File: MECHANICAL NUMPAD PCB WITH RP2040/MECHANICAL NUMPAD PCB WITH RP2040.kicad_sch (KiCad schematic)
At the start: 77 parts, among them IC2 RP2040_QFN56, SW1 SW_Push, SW10 SW_Push, SW11 SW_Push, SW12 SW_Push, SW13 SW_Push, SW14 SW_Push, SW15 SW_Push, SW16 SW_Push, SW17 SW_Push, SW18 SW_Push, SW19 SW_Push, SW2 SW_Push, SW20 SW_Push, SW21 KMR2, SW22 KMR2, SW3 SW_Push, SW4 SW_Push, SW5 SW_Push, SW6 SW_Push, SW7 SW_Push, SW8 SW_Push, SW9 SW_Push, U2 AP2112K-3.3, U5 8MB QSPI Flash, X6 USB TYPE C, Y1 12MHZ

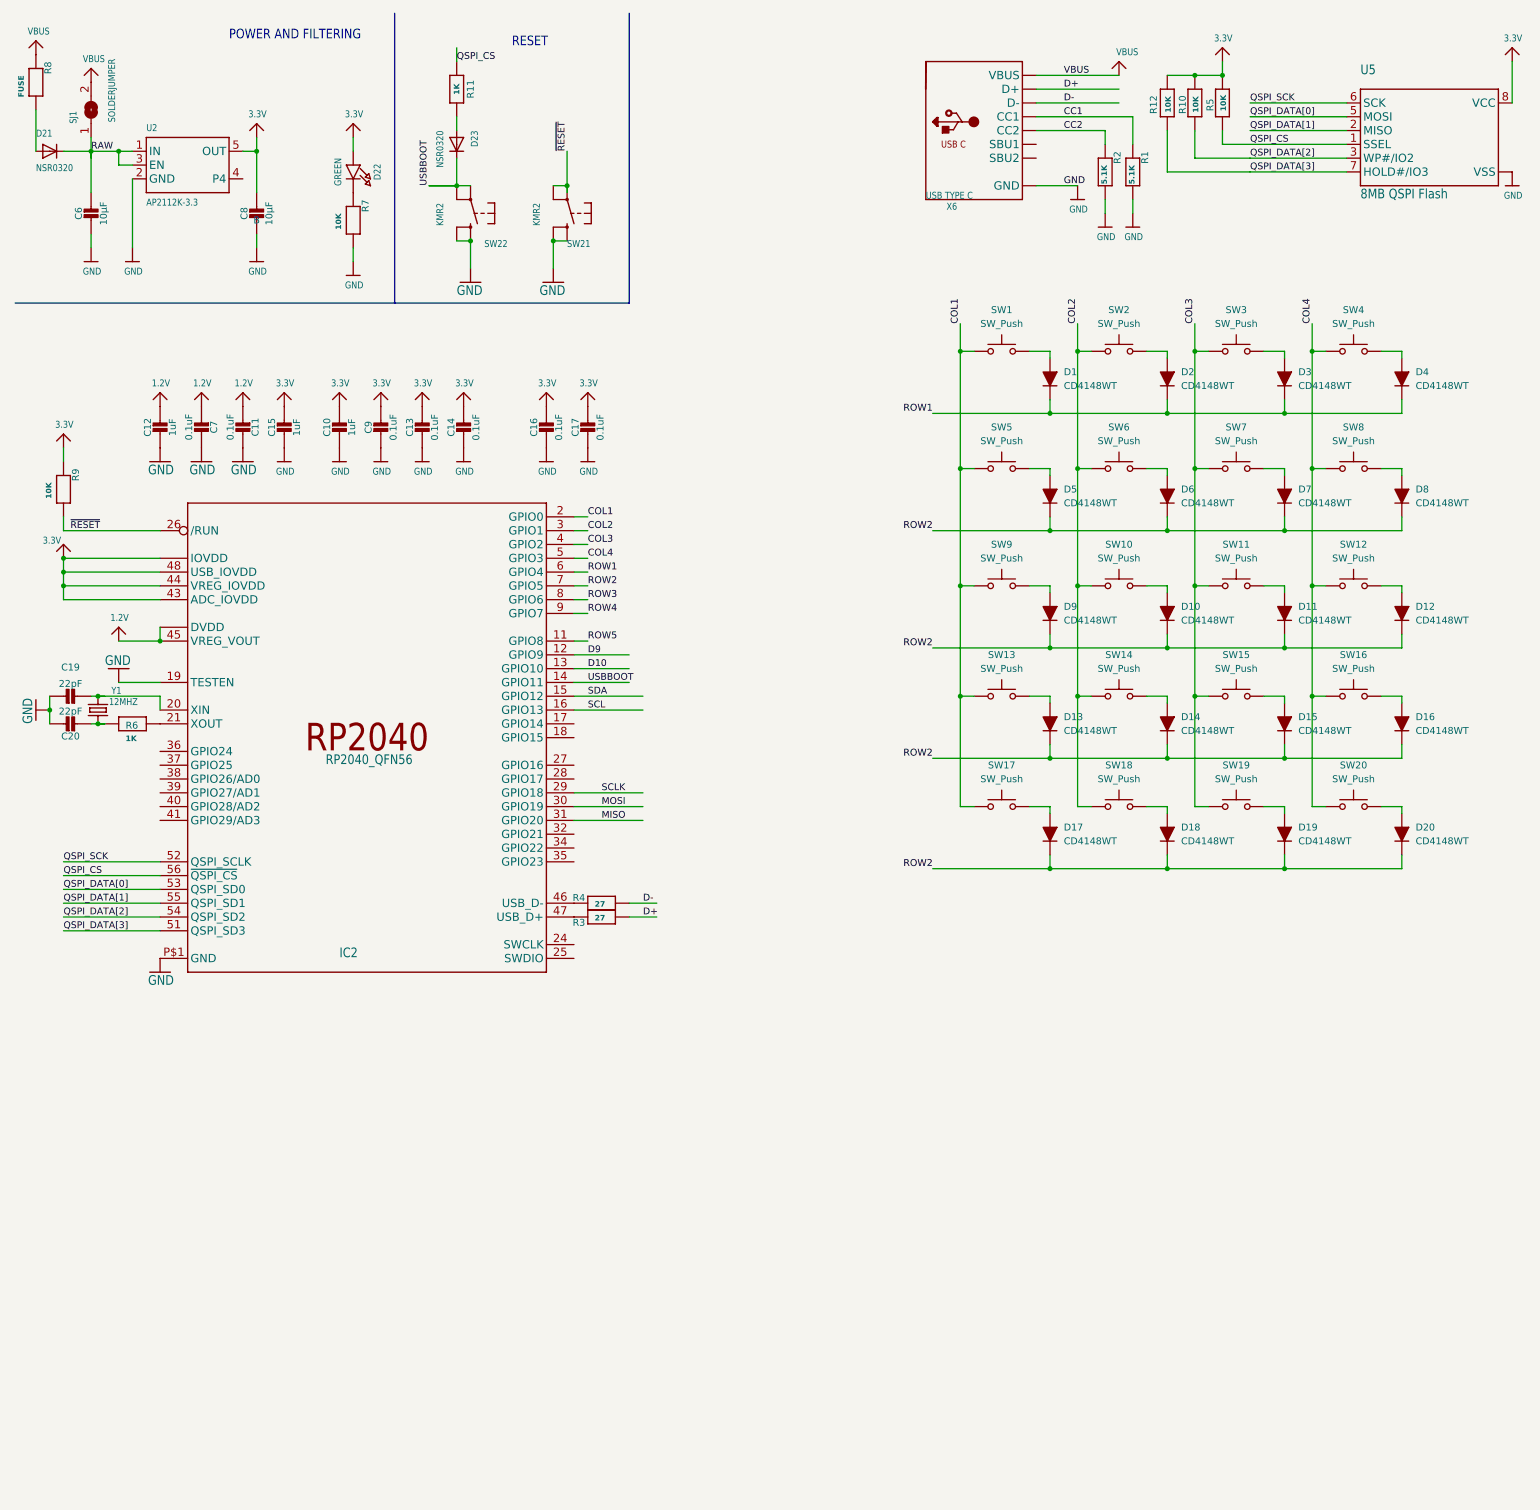
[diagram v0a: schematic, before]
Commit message: Added footprints
Assigned footprints to all components, learned about bulk schematic symbol editing
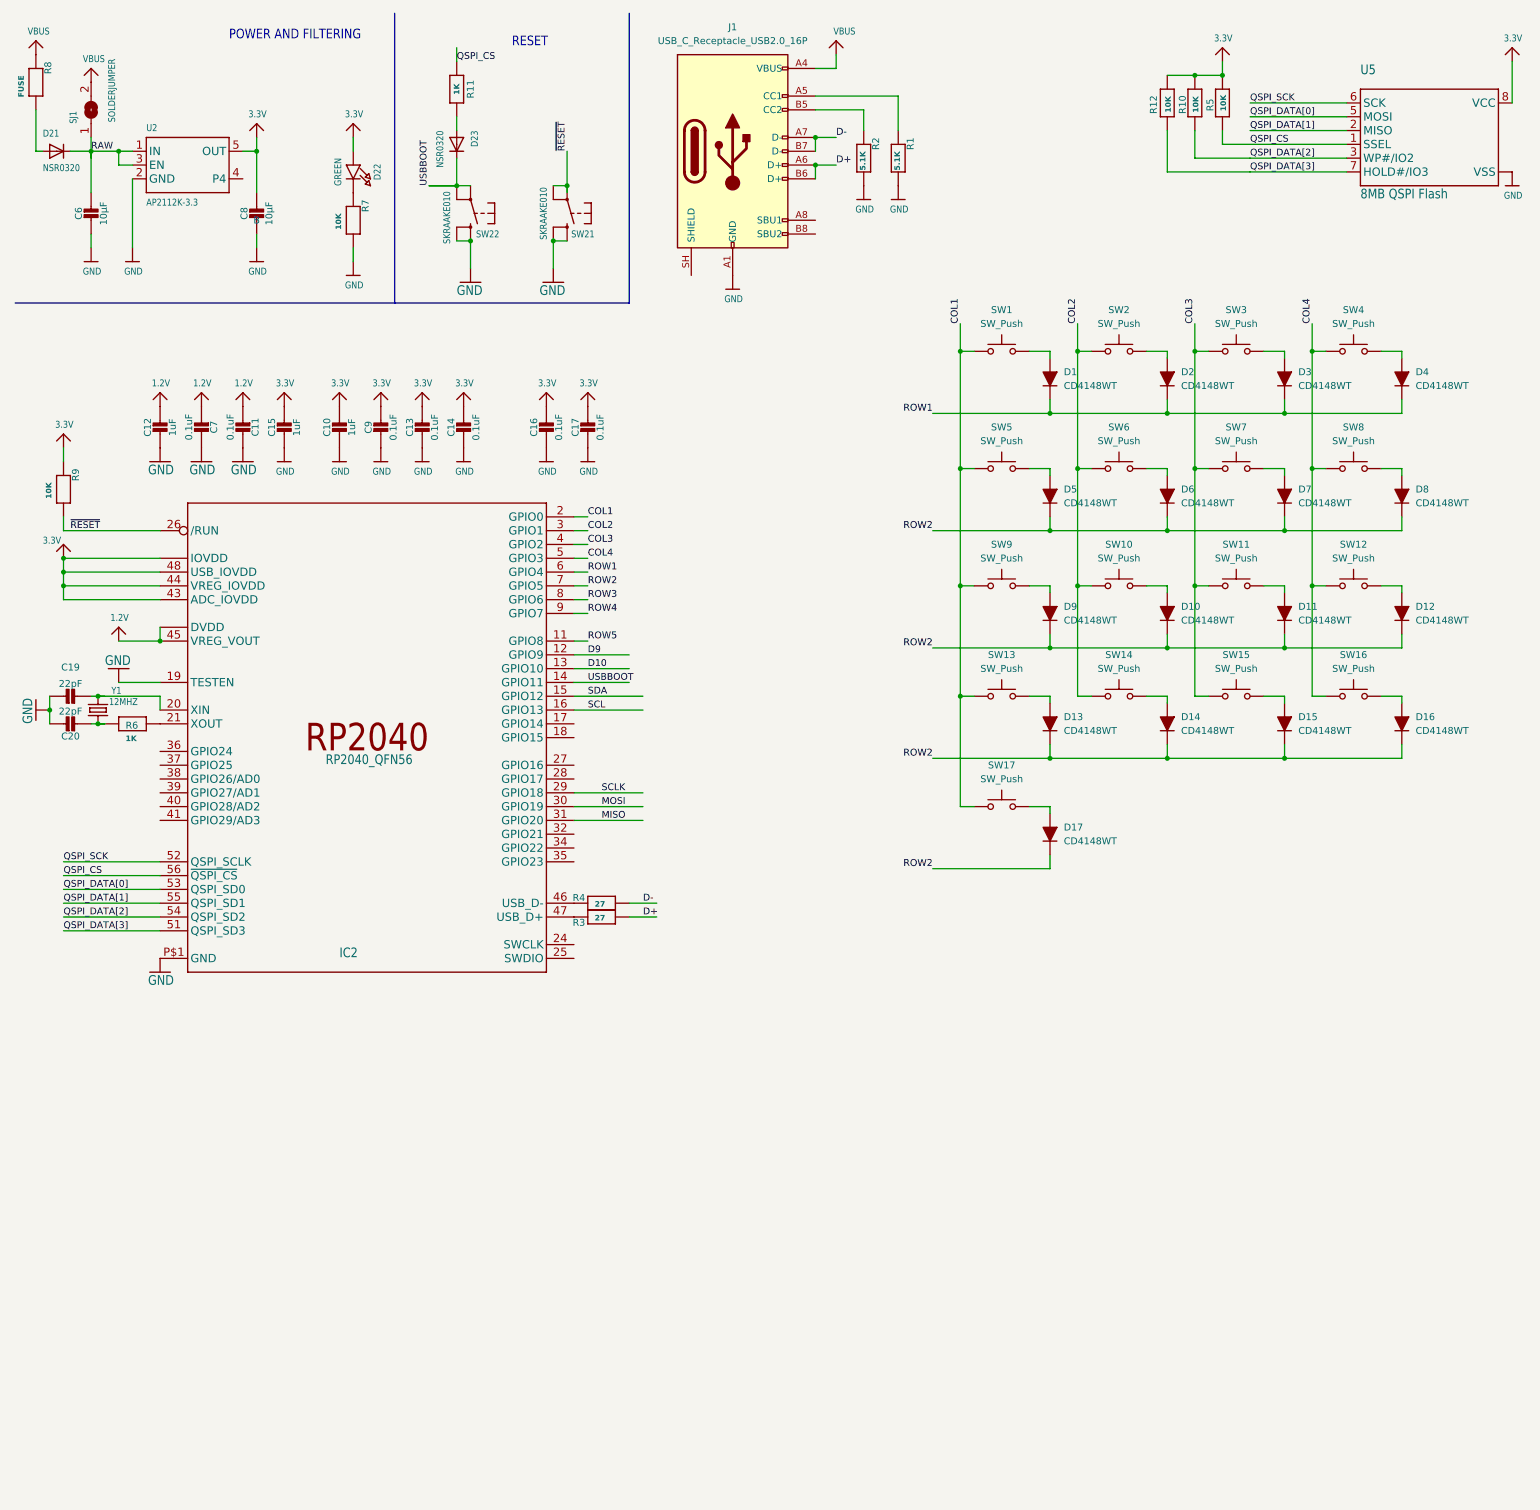
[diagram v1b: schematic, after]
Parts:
- removed D18, D19, D20: CD4148WT, PCM_Diode_SMD_AKL:D_0603_1608Metric, symbol PCM_Diode_AKL:CD4148WT
- removed SW18, SW19, SW20: SW_Push, PCM_Switch_Keyboard_Hotswap_Kailh:SW_Hotswap_Kailh_MX_1.00u, symbol Switch:SW_Push
- removed X6: USB TYPE C, Adafruit KB2040:USB_C_CUSB31-CFM2AX-01-X, symbol Adafruit KB2040-eagle-import:USB_C
- added J1: USB_C_Receptacle_USB2.0_16P, Connector_USB:USB_C_Receptacle_GCT_USB4105-xx-A_16P_TopMnt_Horizontal, symbol Connector:USB_C_Receptacle_USB2.0_16P
- C10, C12: footprint Adafruit KB2040:_0603MP -> Capacitor_SMD:C_0805_2012Metric
- C11, C13, C14, C16, C17, C19, C20, C7, C9: footprint Adafruit KB2040:_0402NO -> Capacitor_SMD:C_0805_2012Metric
- C15: footprint Adafruit KB2040:0603-NO -> Capacitor_SMD:C_0805_2012Metric
- C6, C8: footprint Adafruit KB2040:_0805MP -> Capacitor_SMD:C_0805_2012Metric
- D1, D10, D11, D12, D13, D14, D15, D16, D17, D2, D3, D4, D5, D6, D7, D8, D9: footprint PCM_Diode_SMD_AKL:D_0603_1608Metric -> PCM_Diode_SMD_AKL:D_0805_2012Metric
- D21, D23: footprint PCM_Diode_SMD_Handsoldering_AKL:D_0603_1608Metric -> PCM_Diode_SMD_AKL:D_0805_2012Metric
- D22: footprint PCM_fab:LED_0603 -> PCM_LED_SMD_AKL:LED_0805_2012Metric
- R1, R10, R11, R12, R2, R3, R4, R5, R6: footprint Adafruit KB2040:_0402NO -> Resistor_SMD:R_0805_2012Metric
- R7, R9: footprint Resistor_SMD:R_0603_1608Metric -> Resistor_SMD:R_0805_2012Metric
- R8: footprint Adafruit KB2040:0805-NO -> Fuse:Fuse_0805_2012Metric
- SJ1: footprint Adafruit KB2040:SOLDERJUMPER_ARROW_NOPASTE -> Jumper:SolderJumper-2_P1.3mm_Open_Pad1.0x1.5mm
- SW21, SW22: value KMR2 -> SKRAAKE010; footprint Adafruit KB2040:BTN_KMR2_4.6X2.8 -> JH_FOOTPRINTS:SW4_SKRAAKE010_ALPS
- U2: footprint Adafruit KB2040:SOT23-5 -> PCM_SparkFun-Semiconductor-Standard:SOT23-5
- U5: footprint Adafruit KB2040:USON8_4X4 -> Package_SON:Texas_R-PUSON-N8_USON-8-1EP_1.6x2.1mm_P0.5mm_EP0.4x1.7mm
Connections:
- net D+: now also J1.A6 (D+), J1.B6 (D+)
- net D-: now also J1.A7 (D-), J1.B7 (D-)
- net GND: now also SW21.2 (S), SW21.4 (S1), SW22.2 (S), SW22.4 (S1), J1.A1 (GND), J1.A12 (GND), J1.B1 (GND), J1.B12 (GND); no longer SW21.B (S), SW21.B' (S1), SW22.B (S), SW22.B' (S1)
- net USBBOOT: now also SW22.1 (P), SW22.3 (P1); no longer SW22.A (P), SW22.A' (P1)
- net VBUS: now also J1.A4 (VBUS), J1.A9 (VBUS), J1.B4 (VBUS), J1.B9 (VBUS)
- net ~{RESET}: now also SW21.1 (P), SW21.3 (P1); no longer SW21.A (P), SW21.A' (P1)
- net CC1: no longer names the net of R1.1
- net CC1: now also J1.A5 (CC1)
- net CC2: no longer names the net of R2.1
- net CC2: now also J1.B5 (CC2)
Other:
- moved on the sheet: D21

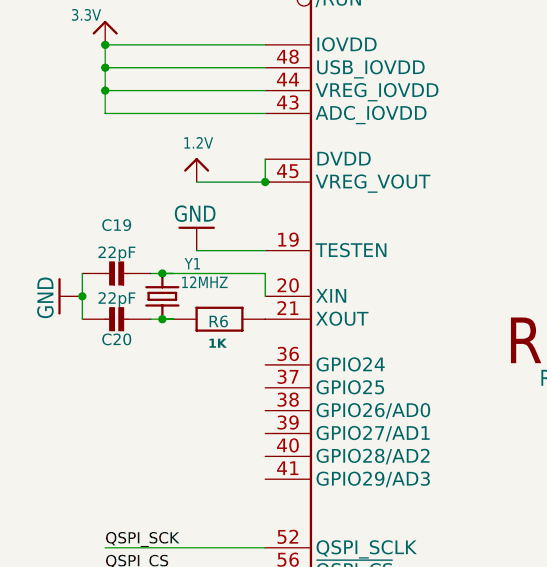
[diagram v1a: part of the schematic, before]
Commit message: Connecting components by matching symbol pin and footprint pad labels
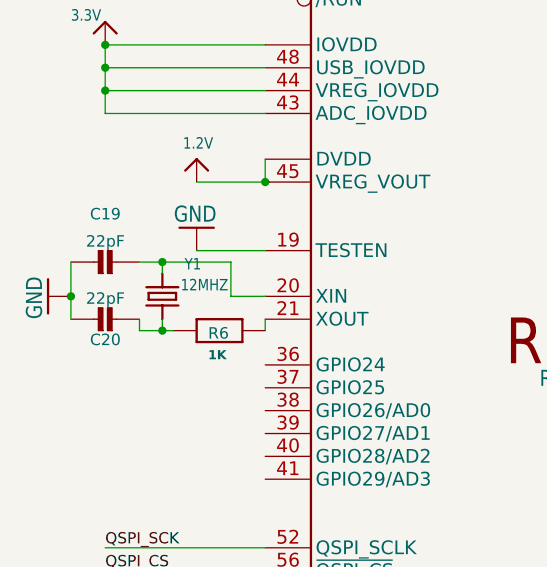
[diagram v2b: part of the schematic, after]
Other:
- moved on the sheet: C19, C20, R6
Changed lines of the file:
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@@
 	)
 	(junction
+		(at 17.78 139.7)
+		(diameter 0)
+		(color 0 0 0 0)
+	)
+	(junction
 		(at 186.69 137.16)
 		(diameter 0)
@@
 	)
 	(junction
-		(at 19.05 139.7)
+		(at 203.2 85.09)
 		(diameter 0)
 		(color 0 0 0 0)
 	)
 	(junction
-		(at 203.2 85.09)
+		(at 27.94 143.51)
 		(diameter 0)
 		(color 0 0 0 0)
@@
 	)
 	(junction
-		(at 27.94 137.16)
-		(diameter 0)
-		(color 0 0 0 0)
-	)
-	(junction
 		(at 186.69 116.84)
 		(diameter 0)
@@
 	)
 	(junction
-		(at 27.94 142.24)
+		(at 27.94 135.89)
 		(diameter 0)
 		(color 0 0 0 0)
@@
 	(wire
 		(pts
+			(xy 35.56 135.89) (xy 35.56 139.7)
+		)
+		(stroke
+			(width 0)
+			(type default)
+		)
+	)
+	(wire
+		(pts
 			(xy 39.37 114.3) (xy 21.59 114.3)
 		)
@@
 	(wire
 		(pts
+			(xy 25.4 143.51) (xy 25.4 142.24)
+		)
+		(stroke
+			(width 0)
+			(type default)
+		)
+	)
+	(wire
+		(pts
 			(xy 111.76 58.42) (xy 111.76 53.34)
 		)
@@
 	(wire
 		(pts
-			(xy 267.97 95.25) (xy 267.97 96.52)
+			(xy 27.94 135.89) (xy 35.56 135.89)
 		)
 		(stroke
@@
 		)
 	)
-	(polyline
-		(pts
-			(xy 82.55 64.77) (xy 125.73 64.77)
-		)
-		(stroke
-			(width 0.1524)
-			(type solid)
-		)
-	)
 	(wire
 		(pts
-			(xy 39.37 137.16) (xy 39.37 139.7)
+			(xy 267.97 95.25) (xy 267.97 96.52)
 		)
 		(stroke
-			(width 0.1524)
-			(type solid)
+			(width 0)
+			(type default)
 		)
 	)
-	(wire
+	(polyline
 		(pts
-			(xy 39.37 134.62) (xy 31.75 134.62)
+			(xy 82.55 64.77) (xy 125.73 64.77)
 		)
 		(stroke
@@
 	(wire
 		(pts
-			(xy 27.94 137.16) (xy 39.37 137.16)
+			(xy 39.37 134.62) (xy 31.75 134.62)
 		)
 		(stroke
@@
 	(wire
 		(pts
+			(xy 35.56 139.7) (xy 39.37 139.7)
+		)
+		(stroke
+			(width 0)
+			(type default)
+		)
+	)
+	(wire
+		(pts
 			(xy 203.2 128.27) (xy 224.79 128.27)
 		)
@@
 	(wire
 		(pts
+			(xy 27.94 135.89) (xy 27.94 137.16)
+		)
+		(stroke
+			(width 0)
+			(type default)
+		)
+	)
+	(wire
+		(pts
 			(xy 21.59 177.8) (xy 39.37 177.8)
 		)
@@
 	(wire
 		(pts
-			(xy 93.98 33.02) (xy 93.98 30.48)
+			(xy 39.37 143.51) (xy 39.37 142.24)
 		)
 		(stroke
-			(width 0.1524)
-			(type solid)
+			(width 0)
+			(type default)
 		)
 	)
 	(wire
 		(pts
-			(xy 242.57 95.25) (xy 246.38 95.25)
+			(xy 93.98 33.02) (xy 93.98 30.48)
 		)
 		(stroke
-			(width 0)
-			(type default)
+			(width 0.1524)
+			(type solid)
 		)
 	)
 	(wire
 		(pts
-			(xy 208.28 95.25) (xy 208.28 116.84)
+			(xy 242.57 95.25) (xy 246.38 95.25)
 		)
 		(stroke
@@
 	(wire
 		(pts
-			(xy 27.94 137.16) (xy 29.21 137.16)
+			(xy 208.28 95.25) (xy 208.28 116.84)
 		)
 		(stroke
@@
 	(wire
 		(pts
+			(xy 27.94 143.51) (xy 29.21 143.51)
+		)
+		(stroke
+			(width 0)
+			(type default)
+		)
+	)
+	(wire
+		(pts
 			(xy 160.02 21.59) (xy 163.83 21.59)
 		)
@@
 	(wire
 		(pts
+			(xy 25.4 135.89) (xy 27.94 135.89)
+		)
+		(stroke
+			(width 0)
+			(type default)
+		)
+	)
+	(wire
+		(pts
 			(xy 267.97 146.05) (xy 267.97 148.59)
 		)
@@
 	(wire
 		(pts
-			(xy 19.05 142.24) (xy 19.05 139.7)
+			(xy 17.78 142.24) (xy 17.78 139.7)
 		)
 		(stroke
@@
 	(wire
 		(pts
-			(xy 26.67 142.24) (xy 27.94 142.24)
-		)
-		(stroke
-			(width 0.1524)
-			(type solid)
-		)
-	)
-	(wire
-		(pts
-			(xy 19.05 139.7) (xy 19.05 137.16)
+			(xy 17.78 139.7) (xy 17.78 135.89)
 		)
 		(stroke
@@
 	(wire
 		(pts
+			(xy 25.4 143.51) (xy 27.94 143.51)
+		)
+		(stroke
+			(width 0)
+			(type default)
+		)
+	)
+	(wire
+		(pts
 			(xy 88.9 43.18) (xy 93.98 43.18)
 		)
@@
 	(wire
 		(pts
+			(xy 27.94 143.51) (xy 27.94 142.24)
+		)
+		(stroke
+			(width 0)
+			(type default)
+		)
+	)
+	(wire
+		(pts
 			(xy 203.2 95.25) (xy 203.2 96.52)
 		)
@@
 	(wire
 		(pts
-			(xy 27.94 142.24) (xy 29.21 142.24)
-		)
-		(stroke
-			(width 0)
-			(type default)
-		)
-	)
-	(wire
-		(pts
 			(xy 264.16 137.16) (xy 267.97 137.16)
 		)
@@
 	(wire
 		(pts
-			(xy 27.94 142.24) (xy 29.21 142.24)
-		)
-		(stroke
-			(width 0.1524)
-			(type solid)
-		)
-	)
-	(wire
-		(pts
 			(xy 267.97 82.55) (xy 267.97 85.09)
 		)
@@
 	(wire
 		(pts
-			(xy 27.94 137.16) (xy 26.67 137.16)
-		)
-		(stroke
-			(width 0.1524)
-			(type solid)
-		)
-	)
-	(wire
-		(pts
 			(xy 186.69 137.16) (xy 189.23 137.16)
 		)
@@
 		)
 		(property "Value" "12MHZ"
-			(at 29.972 138.938 90)
+			(at 29.972 139.192 90)
 			(show_name no)
 			(do_not_autoplace no)
@@
 	(symbol
 		(lib_id "Adafruit KB2040-eagle-import:supply1_371_GND")
-		(at 16.51 139.7 270)
+		(at 15.24 139.7 270)
 		(mirror x)
 		(unit 1)
@@
 		(dnp no)
 		(property "Reference" "#GND31"
-			(at 16.51 139.7 0)
+			(at 15.24 139.7 0)
 			(hide yes)
 			(show_name no)
@@
 		)
 		(property "Value" "GND"
-			(at 13.97 142.24 0)
+			(at 12.7 142.24 0)
 			(show_name no)
 			(do_not_autoplace no)
@@
 		)
 		(property "Footprint" ""
-			(at 16.51 139.7 0)
+			(at 15.24 139.7 0)
 			(hide yes)
 			(show_name no)
@@
 		)
 		(property "Datasheet" ""
-			(at 16.51 139.7 0)
+			(at 15.24 139.7 0)
 			(hide yes)
 			(show_name no)
@@
 		)
 		(property "Description" ""
-			(at 16.51 139.7 0)
+			(at 15.24 139.7 0)
 			(hide yes)
 			(show_name no)
@@
 	(symbol
 		(lib_id "Adafruit KB2040-eagle-import:CAP_CERAMIC_0402NO")
-		(at 24.13 142.24 90)
+		(at 22.86 142.24 90)
 		(unit 1)
 		(body_style 1)
@@
 		(dnp no)
 		(property "Reference" "C20"
-			(at 22.88 144.53 90)
+			(at 21.61 144.53 90)
 			(show_name no)
 			(do_not_autoplace no)
@@
 		)
 		(property "Value" "22pF"
-			(at 22.88 139.94 90)
+			(at 21.61 139.94 90)
 			(show_name no)
 			(do_not_autoplace no)
@@
 		)
 		(property "Footprint" "Capacitor_SMD:C_0805_2012Metric"
-			(at 24.13 142.24 0)
+			(at 22.86 142.24 0)
 			(hide yes)
 			(show_name no)
@@
 		)
 		(property "Datasheet" ""
-			(at 24.13 142.24 0)
+			(at 22.86 142.24 0)
 			(hide yes)
 			(show_name no)
@@
 		)
 		(property "Description" ""
-			(at 24.13 142.24 0)
+			(at 22.86 142.24 0)
 			(hide yes)
 			(show_name no)
@@
 	(symbol
 		(lib_id "Adafruit KB2040-eagle-import:RESISTOR_0402NO")
-		(at 34.29 142.24 0)
+		(at 34.29 143.51 0)
 		(unit 1)
 		(body_style 1)
@@
 		(dnp no)
 		(property "Reference" "R6"
-			(at 33.02 143.2814 0)
+			(at 33.02 144.5514 0)
 			(show_name no)
 			(do_not_autoplace no)
@@
 		)
 		(property "Value" "1K"
-			(at 33.02 145.542 0)
+			(at 33.02 146.812 0)
 			(show_name no)
 			(do_not_autoplace no)
@@
 		)
 		(property "Footprint" "Resistor_SMD:R_0805_2012Metric"
-			(at 34.29 142.24 0)
+			(at 34.29 143.51 0)
 			(hide yes)
 			(show_name no)
@@
 		)
 		(property "Datasheet" ""
-			(at 34.29 142.24 0)
+			(at 34.29 143.51 0)
 			(hide yes)
 			(show_name no)
@@
 		)
 		(property "Description" ""
-			(at 34.29 142.24 0)
+			(at 34.29 143.51 0)
 			(hide yes)
 			(show_name no)
@@
 	(symbol
 		(lib_id "Adafruit KB2040-eagle-import:CAP_CERAMIC_0402NO")
-		(at 24.13 137.16 90)
+		(at 22.86 135.89 90)
 		(unit 1)
 		(body_style 1)
@@
 		(dnp no)
 		(property "Reference" "C19"
-			(at 22.88 131.83 90)
+			(at 21.61 130.56 90)
 			(show_name no)
 			(do_not_autoplace no)
@@
 		)
 		(property "Value" "22pF"
-			(at 22.88 134.86 90)
+			(at 21.61 133.59 90)
 			(show_name no)
 			(do_not_autoplace no)
@@
 		)
 		(property "Footprint" "Capacitor_SMD:C_0805_2012Metric"
-			(at 24.13 137.16 0)
+			(at 22.86 135.89 0)
 			(hide yes)
 			(show_name no)
@@
 		)
 		(property "Datasheet" ""
-			(at 24.13 137.16 0)
+			(at 22.86 135.89 0)
 			(hide yes)
 			(show_name no)
@@
 		)
 		(property "Description" ""
-			(at 24.13 137.16 0)
+			(at 22.86 135.89 0)
 			(hide yes)
 			(show_name no)

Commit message: Refinement of schematic and PCB
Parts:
- C10, C11, C12, C13, C14, C15, C16, C17, C19, C20, C6, C7, C8, C9: footprint Capacitor_SMD:C_0805_2012Metric -> Capacitor_SMD:C_0603_1608Metric
- D1, D10, D11, D12, D13, D14, D15, D16, D17, D2, D3, D4, D5, D6, D7, D8, D9: value CD4148WT -> TS4148; symbol PCM_Diode_AKL:CD4148WT -> PCM_Diode_AKL:CD4148WS
- D21, D23: value NSR0320 -> TS4148; symbol Adafruit KB2040-eagle-import:DIODESOD-323F -> PCM_Diode_AKL:CD4148WS
- D22: footprint PCM_LED_SMD_AKL:LED_0805_2012Metric -> PCM_SparkFun-LED:LED_0603_1608Metric_Green
- R1, R10, R11, R12, R2, R3, R4, R5, R6, R7, R9: footprint Resistor_SMD:R_0805_2012Metric -> Resistor_SMD:R_0603_1608Metric
- R8: footprint Fuse:Fuse_0805_2012Metric -> Fuse:Fuse_0603_1608Metric
- U5: footprint Package_SON:Texas_R-PUSON-N8_USON-8-1EP_1.6x2.1mm_P0.5mm_EP0.4x1.7mm -> PCM_SparkFun-Semiconductor-Standard:USON-8_3x2mm-SkinnyCenterPad
- Y1: footprint Crystal:Crystal_SMD_Abracon_ABM3-2Pin_5.0x3.2mm_HandSoldering -> Crystal:Crystal_SMD_3215-2Pin_3.2x1.5mm
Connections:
- net 3.3V: now also D22.1 (A); no longer D22.A
- net GND: now also IC2.57 (GND), J1.SH (SHIELD), U5.9 (CTRPAD); no longer IC2.P$1 (GND), U5.PAD (VSS)
- net RAW: now also D21.1 (K); no longer D21.C
- net ROW1: no longer D4.1 (K)
- net at C19.2, IC2.20 (XIN): now also Y1.2; no longer Y1.3 (2)
- net at R11.2: now also D23.2 (A); no longer D23.A
- net at R8.2: now also D21.2 (A); no longer D21.A
- net at R7.1: now also D22.2 (C); no longer D22.C
- net at D4.2 (A): no longer SW4.2
- net USBBOOT renamed USB_BOOT
- net USB_BOOT: now also D23.1 (K); no longer D23.C
- no-connect marks 0 -> 18
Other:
- moved on the sheet: C20, D1, D10, D11, D12, D13, D14, D15, D16, D17, D2, D3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
